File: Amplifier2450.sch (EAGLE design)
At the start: 25 parts, among them IC1 7805DT, Q1 FDN360P, X1 SMA-142-0701-801/806, X2 SMA-142-0701-801/806

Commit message: (Tobias): selected components and started the layout
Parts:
- D1, D3: value PD3S160 -> SCHOTTKY_DIODE_; device diode:PD3S160 -> own_htl3r-discrete-1:SCHOTTKY_DIODE_
- L1: value 18n -> 15n; device rcl:L-USL1812 -> own_htl3r-discrete-1:L_US_
- Q1: value FDN360P -> P-KANAL_MOSFET_; device transistor-power:FDN360P -> own_htl3r-discrete-1:P-KANAL_MOSFET_
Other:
- note added: "L1 ... chose an actual 15nH because the Inductance will rise a little at 2.45GHz where it is about 18nH what we actually want"
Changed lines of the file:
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@@
 <part name="P+2" library="supply1" library_urn="urn:adsk.eagle:library:371" deviceset="+15V" device="" value="+V"/>
 <part name="U$2" library="HMC789ST89E" deviceset="HMC789ST89E" device=""/>
-<part name="L1" library="rcl" library_urn="urn:adsk.eagle:library:334" deviceset="L-US" device="L1812" package3d_urn="urn:adsk.eagle:package:23494/2" value="18n"/>
+<part name="L1" library="own_htl3r-discrete-1" deviceset="L_US_" device="" value="15n"/>
 <part name="GND3" library="supply1" library_urn="urn:adsk.eagle:library:371" deviceset="GND" device=""/>
 <part name="GND4" library="supply1" library_urn="urn:adsk.eagle:library:371" deviceset="GND" device=""/>
@@
 <part name="GND10" library="supply1" library_urn="urn:adsk.eagle:library:371" deviceset="GND" device=""/>
 <part name="GND11" library="supply1" library_urn="urn:adsk.eagle:library:371" deviceset="GND" device=""/>
-<part name="D1" library="diode" library_urn="urn:adsk.eagle:library:210" deviceset="PD3S160" device="" package3d_urn="urn:adsk.eagle:package:43459/1"/>
-<part name="Q1" library="transistor-power" library_urn="urn:adsk.eagle:library:400" deviceset="FDN360P" device="" package3d_urn="urn:adsk.eagle:package:29529/2"/>
+<part name="D1" library="own_htl3r-discrete-1" deviceset="SCHOTTKY_DIODE_" device=""/>
+<part name="Q1" library="own_htl3r-discrete-1" deviceset="P-KANAL_MOSFET_" device=""/>
 <part name="R2" library="rcl" library_urn="urn:adsk.eagle:library:334" deviceset="R-EU_" device="R0805" package3d_urn="urn:adsk.eagle:package:23553/2"/>
 <part name="D2" library="diode" library_urn="urn:adsk.eagle:library:210" deviceset="BZX84CSMD" device="" package3d_urn="urn:adsk.eagle:package:43403/2"/>
 <part name="FRAME1" library="frames" library_urn="urn:adsk.eagle:library:229" deviceset="A4L-LOC" device=""/>
-<part name="D3" library="diode" library_urn="urn:adsk.eagle:library:210" deviceset="PD3S160" device="" package3d_urn="urn:adsk.eagle:package:43459/1"/>
+<part name="D3" library="own_htl3r-discrete-1" deviceset="SCHOTTKY_DIODE_" device=""/>
 </parts>
 <sheets>
@@
 <text x="35.56" y="149.86" size="1.778" layer="91" grouprefs="POWERINPUT">Protection against false polarity</text>
 <text x="165.1" y="12.7" size="1.778" layer="91">Tobias Wallner - Juan Carlos Hernandez</text>
+<text x="187.96" y="81.28" size="1.778" layer="91">L1 ... chose an actual 15nH because the
+Inductance will rise a little at 2.45GHz
+where it is about 18nH what we actually
+want</text>
 </plain>
 <instances>
@@
 <attribute name="VALUE" x="159.258" y="61.214" size="1.778" layer="96"/>
 </instance>
-<instance part="L1" gate="G$1" x="182.88" y="81.28" smashed="yes" grouprefs="AMPLIFIER">
-<attribute name="NAME" x="181.61" y="76.2" size="1.778" layer="95" rot="R90"/>
-<attribute name="VALUE" x="186.69" y="76.2" size="1.778" layer="96" rot="R90"/>
+<instance part="L1" gate="G$1" x="182.88" y="86.36" smashed="yes" rot="R270" grouprefs="AMPLIFIER">
+<attribute name="NAME" x="177.8" y="87.63" size="1.778" layer="95"/>
+<attribute name="VALUE" x="177.8" y="82.55" size="1.778" layer="96"/>
 </instance>
 <instance part="GND3" gate="1" x="205.74" y="45.72" smashed="yes" grouprefs="AMPLIFIER">
@@
 <attribute name="VALUE" x="223.52" y="53.34" size="1.778" layer="96"/>
 </instance>
-<instance part="D1" gate="G$1" x="63.5" y="68.58" smashed="yes" rot="R180" grouprefs="DC-DC_CONVERTER">
-<attribute name="NAME" x="65.786" y="66.675" size="1.778" layer="95" rot="R180"/>
-<attribute name="VALUE" x="65.786" y="72.009" size="1.778" layer="96" rot="R180"/>
-</instance>
-<instance part="Q1" gate="G$1" x="50.8" y="139.7" smashed="yes" rot="MR90" grouprefs="POWERINPUT">
-<attribute name="NAME" x="53.34" y="146.05" size="1.778" layer="95" rot="MR90"/>
-<attribute name="VALUE" x="49.53" y="144.78" size="1.778" layer="96" rot="MR0"/>
+<instance part="D1" gate="G$1" x="66.04" y="68.58" smashed="yes" rot="R180" grouprefs="DC-DC_CONVERTER">
+<attribute name="NAME" x="68.326" y="66.675" size="1.778" layer="95" rot="R180"/>
+<attribute name="VALUE" x="68.326" y="72.009" size="1.778" layer="96" rot="R180"/>
+</instance>
+<instance part="Q1" gate="G$1" x="50.8" y="142.24" smashed="yes" rot="MR90" grouprefs="POWERINPUT">
+<attribute name="NAME" x="53.34" y="148.59" size="1.778" layer="95" rot="MR90"/>
+<attribute name="VALUE" x="49.53" y="147.32" size="1.778" layer="96" rot="MR0"/>
 </instance>
 <instance part="R2" gate="G$1" x="53.34" y="124.46" smashed="yes" rot="R90" grouprefs="POWERINPUT">
@@
 <junction x="53.34" y="116.84" grouprefs="POWERINPUT"/>
 <pinref part="D3" gate="G$1" pin="A"/>
-<wire x1="66.04" y1="124.46" x2="66.04" y2="116.84" width="0.1524" layer="91"/>
+<wire x1="66.04" y1="127" x2="66.04" y2="116.84" width="0.1524" layer="91"/>
 <junction x="66.04" y="116.84"/>
 </segment>
@@
 <junction x="60.96" y="142.24" grouprefs="POWERINPUT"/>
 <pinref part="D3" gate="G$1" pin="C"/>
-<wire x1="66.04" y1="129.54" x2="66.04" y2="142.24" width="0.1524" layer="91"/>
+<wire x1="66.04" y1="132.08" x2="66.04" y2="142.24" width="0.1524" layer="91"/>
 <junction x="66.04" y="142.24"/>
 </segment>
@@
 <pinref part="L1" gate="G$1" pin="1"/>
 <pinref part="C4" gate="G$1" pin="1"/>
-<wire x1="182.88" y1="88.9" x2="182.88" y2="96.52" width="0.1524" layer="91" grouprefs="AMPLIFIER"/>
+<wire x1="182.88" y1="91.44" x2="182.88" y2="96.52" width="0.1524" layer="91" grouprefs="AMPLIFIER"/>
 <wire x1="182.88" y1="96.52" x2="193.04" y2="96.52" width="0.1524" layer="91" grouprefs="AMPLIFIER"/>
 <pinref part="C5" gate="G$1" pin="1"/>
@@
 <wire x1="177.8" y1="66.04" x2="182.88" y2="66.04" width="0.1524" layer="91" grouprefs="AMPLIFIER"/>
 <pinref part="L1" gate="G$1" pin="2"/>
-<wire x1="182.88" y1="73.66" x2="182.88" y2="66.04" width="0.1524" layer="91" grouprefs="AMPLIFIER"/>
+<wire x1="182.88" y1="78.74" x2="182.88" y2="66.04" width="0.1524" layer="91" grouprefs="AMPLIFIER"/>
 <pinref part="C3" gate="G$1" pin="1"/>
 <wire x1="182.88" y1="66.04" x2="193.04" y2="66.04" width="0.1524" layer="91" grouprefs="AMPLIFIER"/>

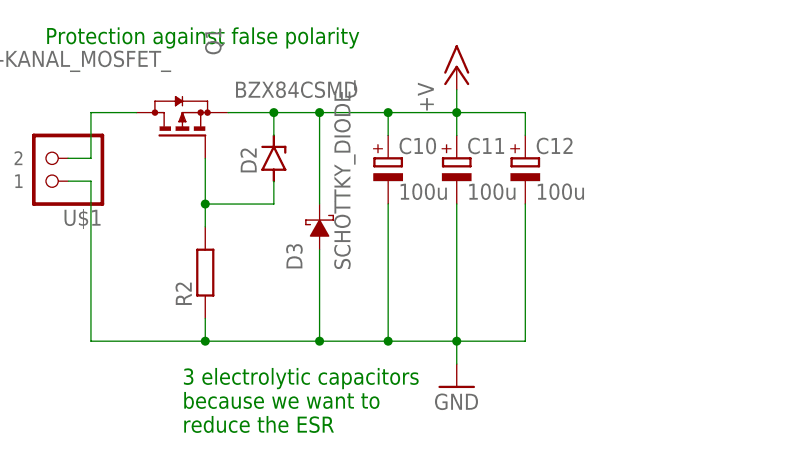
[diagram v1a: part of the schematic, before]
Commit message: (Tobias): added a top layer ground plane cutout around the signal line to prevent spilling.
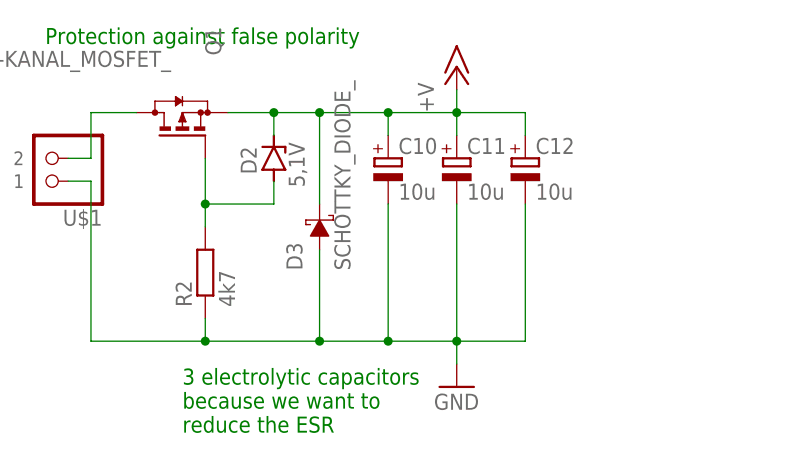
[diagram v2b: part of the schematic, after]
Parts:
- C10, C11, C12: value 100u -> 10u
- D2: value BZX84CSMD -> 5,1V; device diode:BZX84CSMD -> diode:ZENER-DIODESOT23
- R2: value (none) -> 4k7
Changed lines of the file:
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@@
 <part name="P+1" library="supply1" library_urn="urn:adsk.eagle:library:371" deviceset="+5V" device=""/>
 <part name="P+3" library="supply1" library_urn="urn:adsk.eagle:library:371" deviceset="+15V" device="" value="+V"/>
-<part name="C10" library="rcl" library_urn="urn:adsk.eagle:library:334" deviceset="CPOL-EU" device="E2.5-5" package3d_urn="urn:adsk.eagle:package:23344/1" value="100u"/>
-<part name="C11" library="rcl" library_urn="urn:adsk.eagle:library:334" deviceset="CPOL-EU" device="E2.5-5" package3d_urn="urn:adsk.eagle:package:23344/1" value="100u"/>
-<part name="C12" library="rcl" library_urn="urn:adsk.eagle:library:334" deviceset="CPOL-EU" device="E2.5-5" package3d_urn="urn:adsk.eagle:package:23344/1" value="100u"/>
+<part name="C10" library="rcl" library_urn="urn:adsk.eagle:library:334" deviceset="CPOL-EU" device="E2.5-5" package3d_urn="urn:adsk.eagle:package:23344/1" value="10u"/>
+<part name="C11" library="rcl" library_urn="urn:adsk.eagle:library:334" deviceset="CPOL-EU" device="E2.5-5" package3d_urn="urn:adsk.eagle:package:23344/1" value="10u"/>
+<part name="C12" library="rcl" library_urn="urn:adsk.eagle:library:334" deviceset="CPOL-EU" device="E2.5-5" package3d_urn="urn:adsk.eagle:package:23344/1" value="10u"/>
 <part name="GND2" library="supply1" library_urn="urn:adsk.eagle:library:371" deviceset="GND" device=""/>
 <part name="P+2" library="supply1" library_urn="urn:adsk.eagle:library:371" deviceset="+15V" device="" value="+V"/>
@@
 <part name="D1" library="own_htl3r-discrete-1" deviceset="SCHOTTKY_DIODE_" device=""/>
 <part name="Q1" library="own_htl3r-discrete-1" deviceset="P-KANAL_MOSFET_" device=""/>
-<part name="R2" library="rcl" library_urn="urn:adsk.eagle:library:334" deviceset="R-EU_" device="R0805" package3d_urn="urn:adsk.eagle:package:23553/2"/>
-<part name="D2" library="diode" library_urn="urn:adsk.eagle:library:210" deviceset="BZX84CSMD" device="" package3d_urn="urn:adsk.eagle:package:43403/2"/>
+<part name="R2" library="rcl" library_urn="urn:adsk.eagle:library:334" deviceset="R-EU_" device="R0805" package3d_urn="urn:adsk.eagle:package:23553/2" value="4k7"/>
+<part name="D2" library="diode" library_urn="urn:adsk.eagle:library:210" deviceset="ZENER-DIODE" device="SOT23" package3d_urn="urn:adsk.eagle:package:43389/2" value="5,1V"/>
 <part name="FRAME1" library="frames" library_urn="urn:adsk.eagle:library:229" deviceset="A4L-LOC" device=""/>
 <part name="D3" library="own_htl3r-discrete-1" deviceset="SCHOTTKY_DIODE_" device=""/>
@@
 <instance part="D2" gate="G$1" x="60.96" y="137.16" smashed="yes" rot="R90" grouprefs="POWERINPUT">
 <attribute name="NAME" x="59.055" y="135.382" size="1.778" layer="95" rot="R90"/>
-<attribute name="VALUE" x="70.358" y="145.669" size="1.778" layer="96" rot="R180"/>
+<attribute name="VALUE" x="62.611" y="138.938" size="1.778" layer="96" rot="R270"/>
 </instance>
 <instance part="FRAME1" gate="G$1" x="0" y="0" smashed="yes">

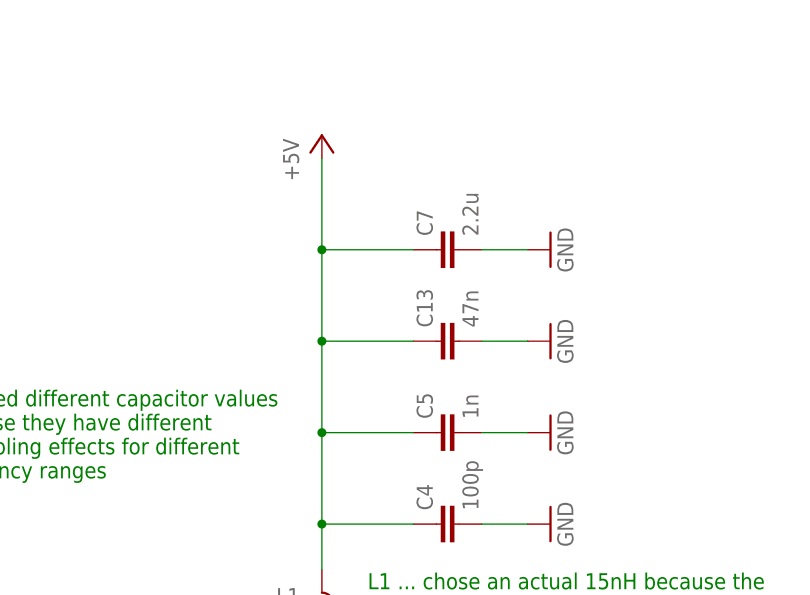
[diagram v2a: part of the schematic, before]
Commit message: (Tobias): started to apply changes from robert 1st meeting
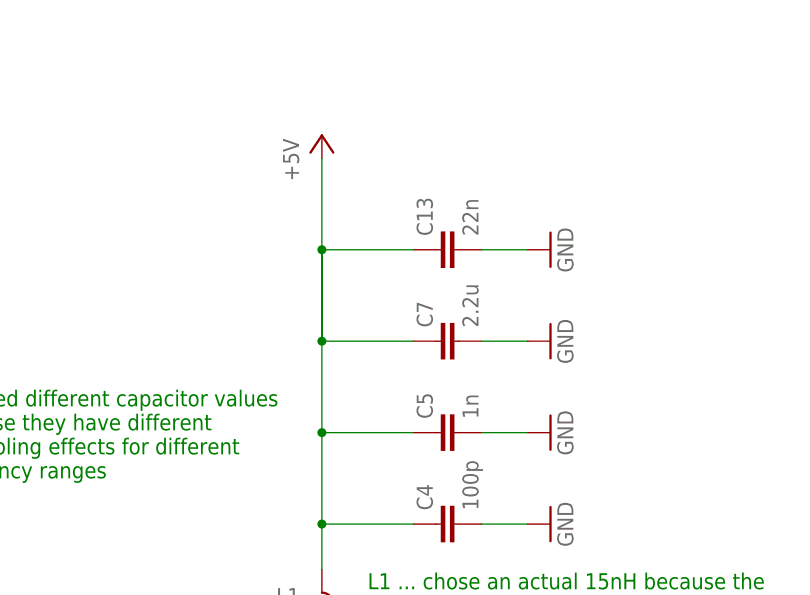
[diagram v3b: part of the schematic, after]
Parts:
- C13: value 47n -> 22n
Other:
- moved on the sheet: C13, C7
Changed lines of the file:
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@@
 <part name="P+4" library="supply1" library_urn="urn:adsk.eagle:library:371" deviceset="+5V" device=""/>
 <part name="R1" library="rcl" library_urn="urn:adsk.eagle:library:334" deviceset="R-EU_" device="R0402" package3d_urn="urn:adsk.eagle:package:23547/3" value="0.0"/>
-<part name="C13" library="rcl" library_urn="urn:adsk.eagle:library:334" deviceset="C-EU" device="C0603" package3d_urn="urn:adsk.eagle:package:23616/2" value="47n"/>
+<part name="C13" library="rcl" library_urn="urn:adsk.eagle:library:334" deviceset="C-EU" device="C0603" package3d_urn="urn:adsk.eagle:package:23616/2" value="22n"/>
 <part name="GND9" library="supply1" library_urn="urn:adsk.eagle:library:371" deviceset="GND" device=""/>
 <part name="X1" library="con-coax" library_urn="urn:adsk.eagle:library:133" deviceset="SMA-" device="142-0701-801/806" package3d_urn="urn:adsk.eagle:package:6214/1"/>
@@
 <attribute name="VALUE" x="207.264" y="53.721" size="1.778" layer="96"/>
 </instance>
-<instance part="C7" gate="G$1" x="195.58" y="127" smashed="yes" rot="R90" grouprefs="AMPLIFIER">
-<attribute name="NAME" x="195.199" y="128.524" size="1.778" layer="95" rot="R90"/>
-<attribute name="VALUE" x="200.279" y="128.524" size="1.778" layer="96" rot="R90"/>
+<instance part="C7" gate="G$1" x="195.58" y="116.84" smashed="yes" rot="R90" grouprefs="AMPLIFIER">
+<attribute name="NAME" x="195.199" y="118.364" size="1.778" layer="95" rot="R90"/>
+<attribute name="VALUE" x="200.279" y="118.364" size="1.778" layer="96" rot="R90"/>
 </instance>
 <instance part="IC1" gate="A1" x="63.5" y="55.88" smashed="yes" grouprefs="DC-DC_CONVERTER">
@@
 <attribute name="VALUE" x="210.82" y="104.14" size="1.778" layer="96" rot="R90"/>
 </instance>
-<instance part="GND8" gate="1" x="208.28" y="127" smashed="yes" rot="R90" grouprefs="AMPLIFIER">
-<attribute name="VALUE" x="210.82" y="124.46" size="1.778" layer="96" rot="R90"/>
+<instance part="GND8" gate="1" x="208.28" y="116.84" smashed="yes" rot="R90" grouprefs="AMPLIFIER">
+<attribute name="VALUE" x="210.82" y="114.3" size="1.778" layer="96" rot="R90"/>
 </instance>
 <instance part="P+4" gate="1" x="182.88" y="139.7" smashed="yes" grouprefs="AMPLIFIER">
@@
 <attribute name="VALUE" x="212.09" y="62.738" size="1.778" layer="96"/>
 </instance>
-<instance part="C13" gate="G$1" x="195.58" y="116.84" smashed="yes" rot="R90" grouprefs="AMPLIFIER">
-<attribute name="NAME" x="195.199" y="118.364" size="1.778" layer="95" rot="R90"/>
-<attribute name="VALUE" x="200.279" y="118.364" size="1.778" layer="96" rot="R90"/>
-</instance>
-<instance part="GND9" gate="1" x="208.28" y="116.84" smashed="yes" rot="R90" grouprefs="AMPLIFIER">
-<attribute name="VALUE" x="210.82" y="114.3" size="1.778" layer="96" rot="R90"/>
+<instance part="C13" gate="G$1" x="195.58" y="127" smashed="yes" rot="R90" grouprefs="AMPLIFIER">
+<attribute name="NAME" x="195.199" y="128.524" size="1.778" layer="95" rot="R90"/>
+<attribute name="VALUE" x="200.279" y="128.524" size="1.778" layer="96" rot="R90"/>
+</instance>
+<instance part="GND9" gate="1" x="208.28" y="127" smashed="yes" rot="R90" grouprefs="AMPLIFIER">
+<attribute name="VALUE" x="210.82" y="124.46" size="1.778" layer="96" rot="R90"/>
 </instance>
 <instance part="X1" gate="G1" x="119.38" y="66.04" smashed="yes" grouprefs="AMPLIFIER">
@@
 <pinref part="C7" gate="G$1" pin="2"/>
 <pinref part="GND8" gate="1" pin="GND"/>
-<wire x1="200.66" y1="127" x2="205.74" y2="127" width="0.1524" layer="91" grouprefs="AMPLIFIER"/>
+<wire x1="200.66" y1="116.84" x2="205.74" y2="116.84" width="0.1524" layer="91" grouprefs="AMPLIFIER"/>
 </segment>
 <segment>
@@
 <pinref part="C13" gate="G$1" pin="2"/>
 <pinref part="GND9" gate="1" pin="GND"/>
-<wire x1="200.66" y1="116.84" x2="205.74" y2="116.84" width="0.1524" layer="91" grouprefs="AMPLIFIER"/>
+<wire x1="200.66" y1="127" x2="205.74" y2="127" width="0.1524" layer="91" grouprefs="AMPLIFIER"/>
 </segment>
 <segment>
@@
 <junction x="182.88" y="96.52" grouprefs="AMPLIFIER"/>
 <pinref part="C7" gate="G$1" pin="1"/>
-<wire x1="193.04" y1="127" x2="182.88" y2="127" width="0.1524" layer="91" grouprefs="AMPLIFIER"/>
-<wire x1="182.88" y1="127" x2="182.88" y2="116.84" width="0.1524" layer="91" grouprefs="AMPLIFIER"/>
+<wire x1="193.04" y1="116.84" x2="182.88" y2="116.84" width="0.1524" layer="91" grouprefs="AMPLIFIER"/>
+<wire x1="182.88" y1="116.84" x2="182.88" y2="127" width="0.1524" layer="91" grouprefs="AMPLIFIER"/>
 <junction x="182.88" y="106.68" grouprefs="AMPLIFIER"/>
-<wire x1="182.88" y1="116.84" x2="182.88" y2="106.68" width="0.1524" layer="91" grouprefs="AMPLIFIER"/>
-<wire x1="182.88" y1="127" x2="182.88" y2="137.16" width="0.1524" layer="91" grouprefs="AMPLIFIER"/>
-<junction x="182.88" y="127" grouprefs="AMPLIFIER"/>
+<wire x1="182.88" y1="127" x2="182.88" y2="106.68" width="0.1524" layer="91" grouprefs="AMPLIFIER"/>
+<wire x1="182.88" y1="116.84" x2="182.88" y2="137.16" width="0.1524" layer="91" grouprefs="AMPLIFIER"/>
+<junction x="182.88" y="116.84" grouprefs="AMPLIFIER"/>
 <pinref part="P+4" gate="1" pin="+5V"/>
 <pinref part="C13" gate="G$1" pin="1"/>
-<wire x1="193.04" y1="116.84" x2="182.88" y2="116.84" width="0.1524" layer="91" grouprefs="AMPLIFIER"/>
-<junction x="182.88" y="116.84" grouprefs="AMPLIFIER"/>
+<wire x1="193.04" y1="127" x2="182.88" y2="127" width="0.1524" layer="91" grouprefs="AMPLIFIER"/>
+<junction x="182.88" y="127" grouprefs="AMPLIFIER"/>
 </segment>
 </net>
